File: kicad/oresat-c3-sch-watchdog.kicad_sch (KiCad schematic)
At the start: 20 parts

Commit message: Rough draft of watchdog and I2C system schematics.
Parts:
- added C112, C113: 10u, symbol Device:C_Small
- added R59: 1k, symbol Device:R_Small_US
- added R60, R61, R64: 100k, symbol Device:R_Small_US
- added R62: 47k, symbol Device:R_Small_US
- added R63: 470k, symbol Device:R_Small_US
- added R65: NP, symbol Device:R_Small_US
- added TP7, TP8, TP9: TestPoint-MinTH, oresat-misc:TestPoint-MinTH, symbol oresat-misc:TestPoint-MinTH
- added U28: TLV1704AIPWR, symbol oresat-ics:TLV1704AIPWR
- R31: value 10 -> 10 (1206)
- R41: value 10k -> 100k
- R58: value 10k -> 1k
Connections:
- net GND: now also C112.1, C113.1, U28.12 (V-)
- net VBUS: now also R65.2
- net at R34.2, R35.1: now also C113.2, U28.10 (-)
- net at R35.2, R36.1: now also U28.6 (-)
- net at R58.1: now also U28.2
- net at C111.2, R41.2, R58.2: now also TP7.1, U28.7 (+)
- net VP: now reaches R36.2, R37.1
- net VP: now also U28.5 (+)
- net VIN: now reaches C107.1, C108.1, C109.1, R31.2, R32.1, R41.1
- net VIN: now also R62.2, U28.3 (V+)
- net at R39.2: now also U28.4 (-)
- net at D3. (2): now also R60.2, R62.1, R63.1, TP9.1, U28.11 (+), U28.14
- net at R32.2, R34.1: now also R61.2
- net WDT renamed PET-WDT
- new net: D3. (2), R64.1
- new net: C112.2, R59.2, R63.2, R64.2, TP8.1, U28.8 (-)
- new net: R60.1, R61.1, U28.9 (+)
- new net: R59.1, U28.1
- new net ~{ORESAT-SD}: R65.1, U28.13
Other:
- note added: "CHANGE PERIOD TO 30 SEC"
- note added: "CHECK FOOTPRINT!!!"
- note added: "DC block and pulse detector"
- note added: "Keeps WDT circuit powered through ~{ORESAT-SD} asserted period (~ 2-3 seconds)"
- note added: "Oscillator"
- note added: "Output buffer"
- note added: "Pulse integrator"
- note removed: "1206"
- moved on the sheet: C107, C108, C109, C110, C111, D1, D3, D9, R31, R32, R34, R35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

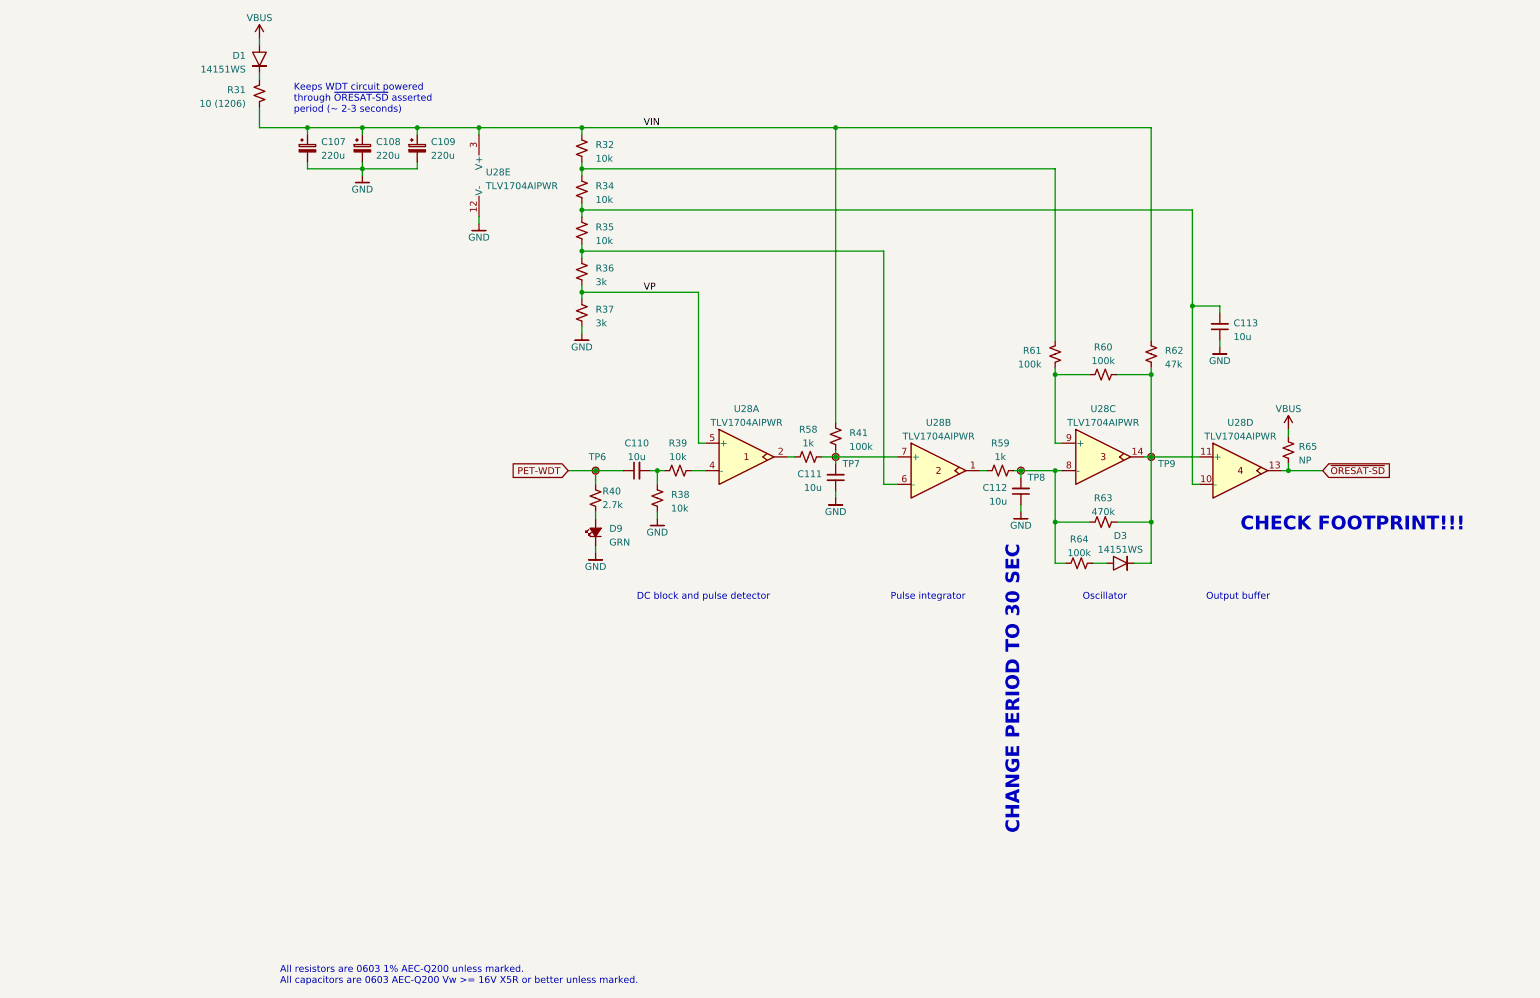
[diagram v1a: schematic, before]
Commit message: Simulated 30 second v6 watchdog circuit and fixed up watchdog in KiCAD.
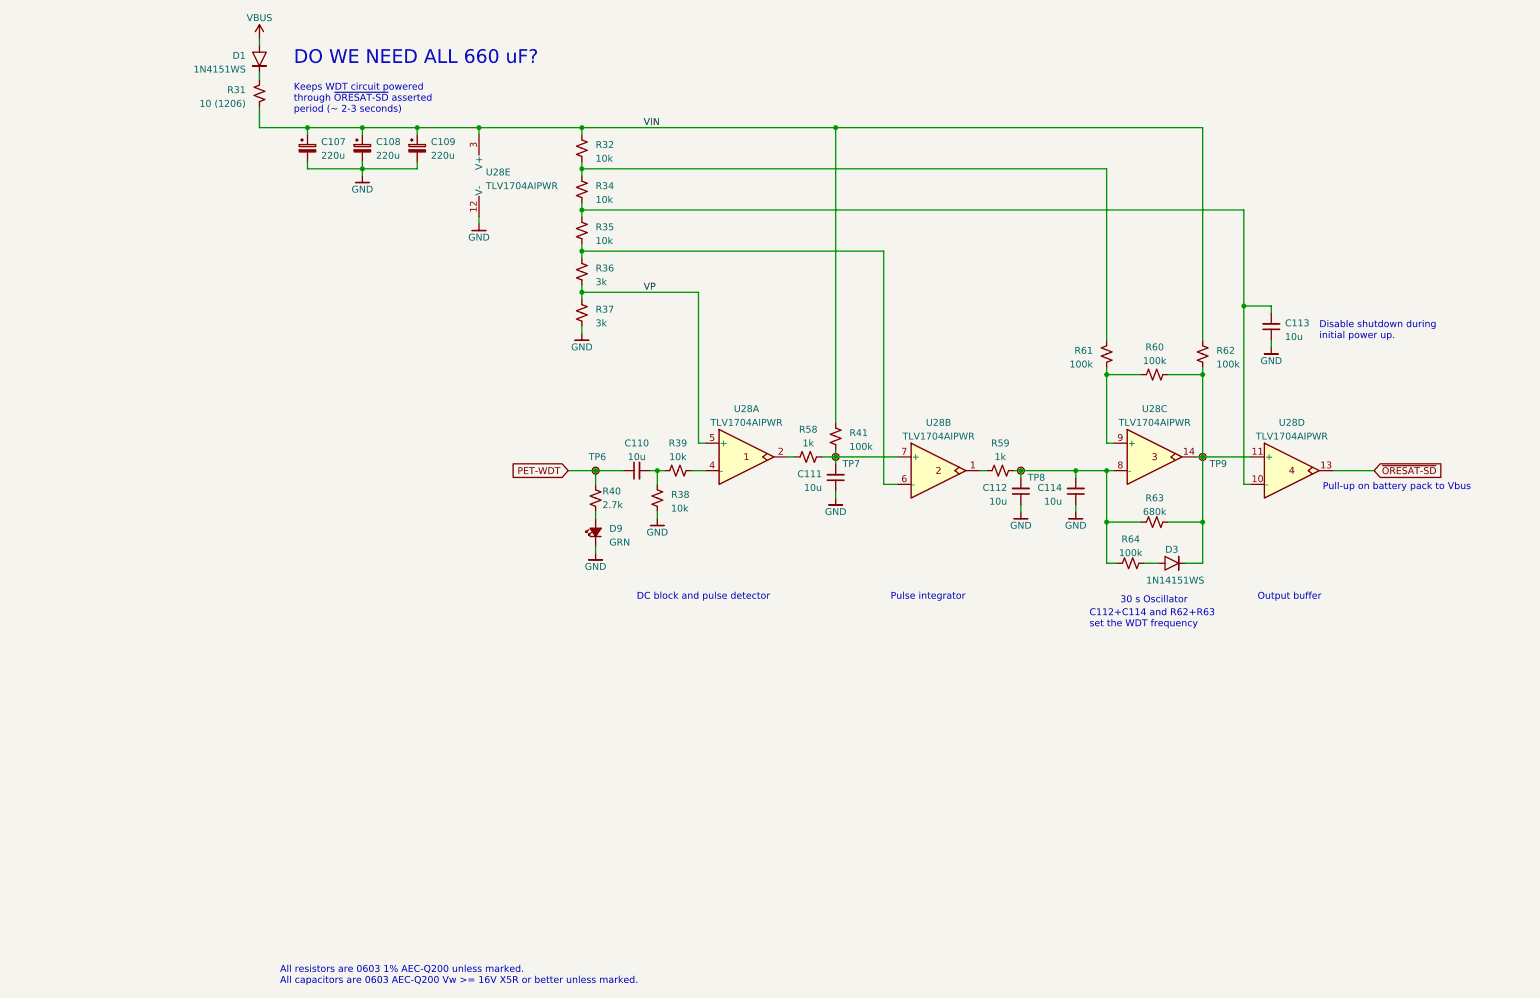
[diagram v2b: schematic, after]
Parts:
- removed R65: NP, symbol Device:R_Small_US
- added C114: 10u, symbol Device:C_Small
- D1: value 14151WS -> 1N4151WS
- D3: value 14151WS -> 1N14151WS
- R62: value 47k -> 100k
- R63: value 470k -> 680k
- U28: footprint (none) -> Package_SO:TSSOP-14_4.4x5mm_P0.65mm
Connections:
- net GND: now also C114.1
- net at C112.2, R59.2, R63.2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: now also C114.2
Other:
- note added: "30 s Oscillator"
- note added: "C112+C114 and R62+R63 set the WDT frequency"
- note added: "DO WE NEED ALL 660 uF?"
- note added: "Disable shutdown during initial power up."
- note added: "Pull-up on battery pack to Vbus"
- note removed: "CHANGE PERIOD TO 30 SEC"
- note removed: "CHECK FOOTPRINT!!!"
- note removed: "Oscillator"
- moved on the sheet: C113, D3, R60, R61, R62, R63, R64, TP9, U28C, U28D

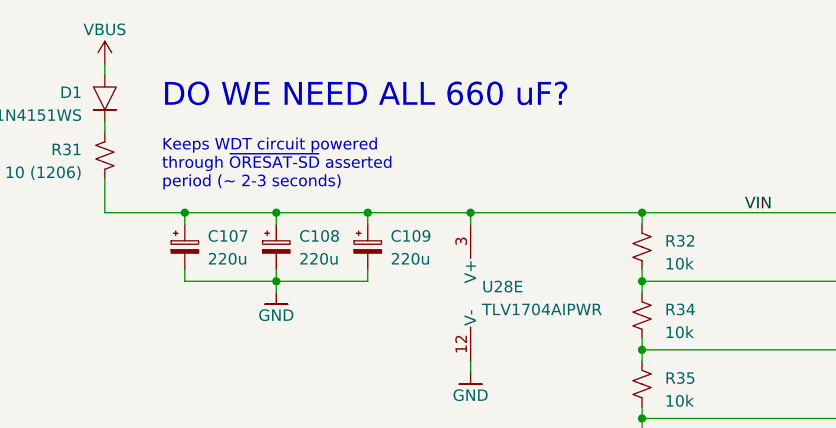
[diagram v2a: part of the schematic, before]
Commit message: C3 v6 schematic now 80% done. OSD2258 IC has been gone over with a fine tooth comb and simplified as much as possible. OSD3358 pinout compared to RED board and PocketBeagle. What's left: lots of little issues, footprints, and then L band and UHF radio schematics need to be fixed.
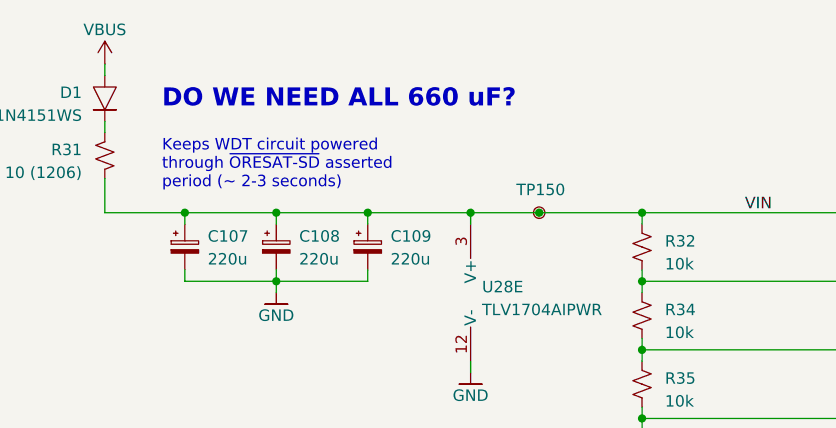
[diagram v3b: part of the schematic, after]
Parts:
- added TP150: TestPoint-MinTH, oresat-misc:TestPoint-MinTH, symbol oresat-misc:TestPoint-MinTH
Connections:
- net VIN: now also TP150.1
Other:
- title: Watchdog Circuit -> OreSat C3: Watchdog Circuit
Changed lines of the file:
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@@
   (paper "B")
   (title_block
-    (title "Watchdog Circuit")
-    (date "2023-05-02")
-    (rev "C3 v6.0")
+    (title "OreSat C3: Watchdog Circuit")
+    (date "2023-05-29")
+    (rev "6.0")
   )
   (junction (at 134.62 109.22) (diameter 0) (color 0 0 0 0)
@@
   (junction (at 272.415 174.625) (diameter 0) (color 0 0 0 0)
   )
+  (junction (at 163.83 101.6) (diameter 0) (color 0 0 0 0)
+  )
   (junction (at 297.815 134.62) (diameter 0) (color 0 0 0 0)
   )
@@
     (stroke (width 0) (type default))
   )
-  (wire (pts (xy 156.21 101.6) (xy 175.26 101.6))
+  (wire (pts (xy 156.21 101.6) (xy 163.83 101.6))
     (stroke (width 0) (type default))
   )
@@
   )
   (wire (pts (xy 175.26 124.46) (xy 231.14 124.46))
+    (stroke (width 0) (type default))
+  )
+  (wire (pts (xy 163.83 101.6) (xy 175.26 101.6))
     (stroke (width 0) (type default))
   )
@@
   )
   (text "DO WE NEED ALL 660 uF?" (at 121.92 90.17 0)
-    (effects (font (size 2.54 2.54) (color 255 0 0 1)) (justify left bottom))
+    (effects (font (size 2 2) (thickness 0.4) bold (color 255 0 0 1)) (justify left bottom))
   )
   (text "All resistors are 0603 1% AEC-Q200 unless marked.\nAll capacitors are 0603 AEC-Q200 Vw >= 16V X5R or better unless marked."
@@
     )
   )
+  (symbol (lib_id "oresat-misc:TestPoint-MinTH") (at 163.83 101.6 0) (unit 1)
+    (in_bom yes) (on_board yes) (dnp no)
+    (property "Reference" "TP150" (at 161.29 99.06 0)
+      (effects (font (size 1.27 1.27)) (justify left))
+    )
+    (property "Value" "TestPoint-MinTH" (at 163.83 94.615 0)
+      (effects (font (size 1.27 1.27)) hide)
+    )
+    (property "Footprint" "oresat-misc:TestPoint-MinTH" (at 163.83 96.52 0)
+      (effects (font (size 1.27 1.27)) hide)
+    )
+    (property "Datasheet" "" (at 163.83 101.6 0)
+      (effects (font (size 1.27 1.27)) hide)
+    )
+    (pin "1")
+    (instances
+      (project "oresat-c3"
+        (path "/65d12cdd-c326-4033-9053-c59fa4e0b25e/730a6f7e-0bbd-44c5-a45a-78e61e54b6d6"
+          (reference "TP150") (unit 1)
+        )
+      )
+    )
+  )
   (symbol (lib_id "Device:R_Small_US") (at 281.305 147.32 90) (unit 1)
     (in_bom yes) (on_board yes) (dnp no) (fields_autoplaced)
@@
     )
   )
-  (symbol (lib_id "oresat-ics:TLV1704AIPWR") (at 205.74 162.56 0) (unit 1)
+  (symbol (lib_name "TLV1704AIPWR_1") (lib_id "oresat-ics:TLV1704AIPWR") (at 205.74 162.56 0) (unit 1)
     (in_bom yes) (on_board yes) (dnp no) (fields_autoplaced)
     (property "Reference" "U28" (at 205.74 153.67 0)

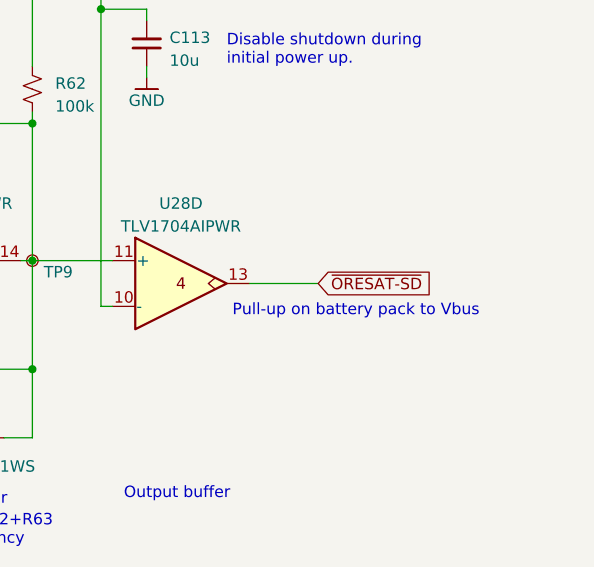
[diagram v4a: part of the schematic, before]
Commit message: Finished UHF radio schematic. Added sheet numbers to external labels. Still to do: L band radio, hooking up GPIO to the OSD3358, and test points.
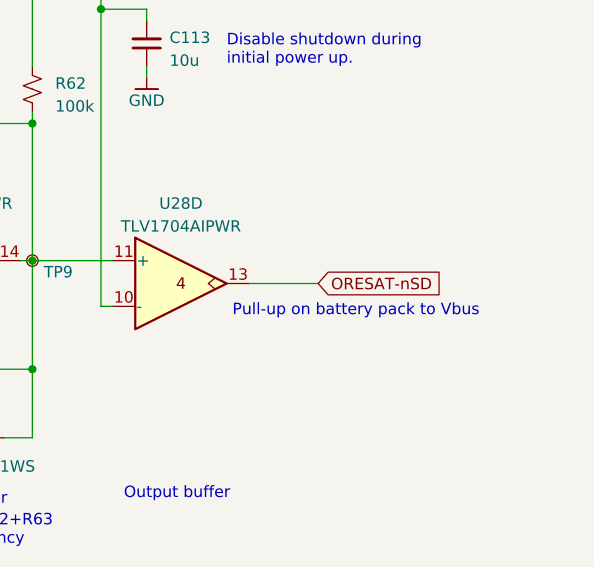
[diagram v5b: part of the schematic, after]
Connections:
- net ~{ORESAT-SD} renamed ORESAT-nSD
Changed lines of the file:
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@@
     (effects (font (size 1.27 1.27)) (justify right))
     (property "Intersheetrefs" "${INTERSHEET_REFS}" (at 161.1662 165.1 0)
-      (effects (font (size 1.27 1.27)) (justify right) hide)
+      (effects (font (size 1.27 1.27)) (justify right))
     )
   )
-  (global_label "~{ORESAT-SD}" (shape input) (at 321.945 165.1 0) (fields_autoplaced)
+  (global_label "ORESAT-nSD" (shape input) (at 321.945 165.1 0) (fields_autoplaced)
     (effects (font (size 1.27 1.27)) (justify left))
-    (property "Intersheetrefs" "${INTERSHEET_REFS}" (at 335.9179 165.1 0)
-      (effects (font (size 1.27 1.27)) (justify left) hide)
+    (property "Intersheetrefs" "${INTERSHEET_REFS}" (at 337.0669 165.1 0)
+      (effects (font (size 1.27 1.27)) (justify left))
     )
   )

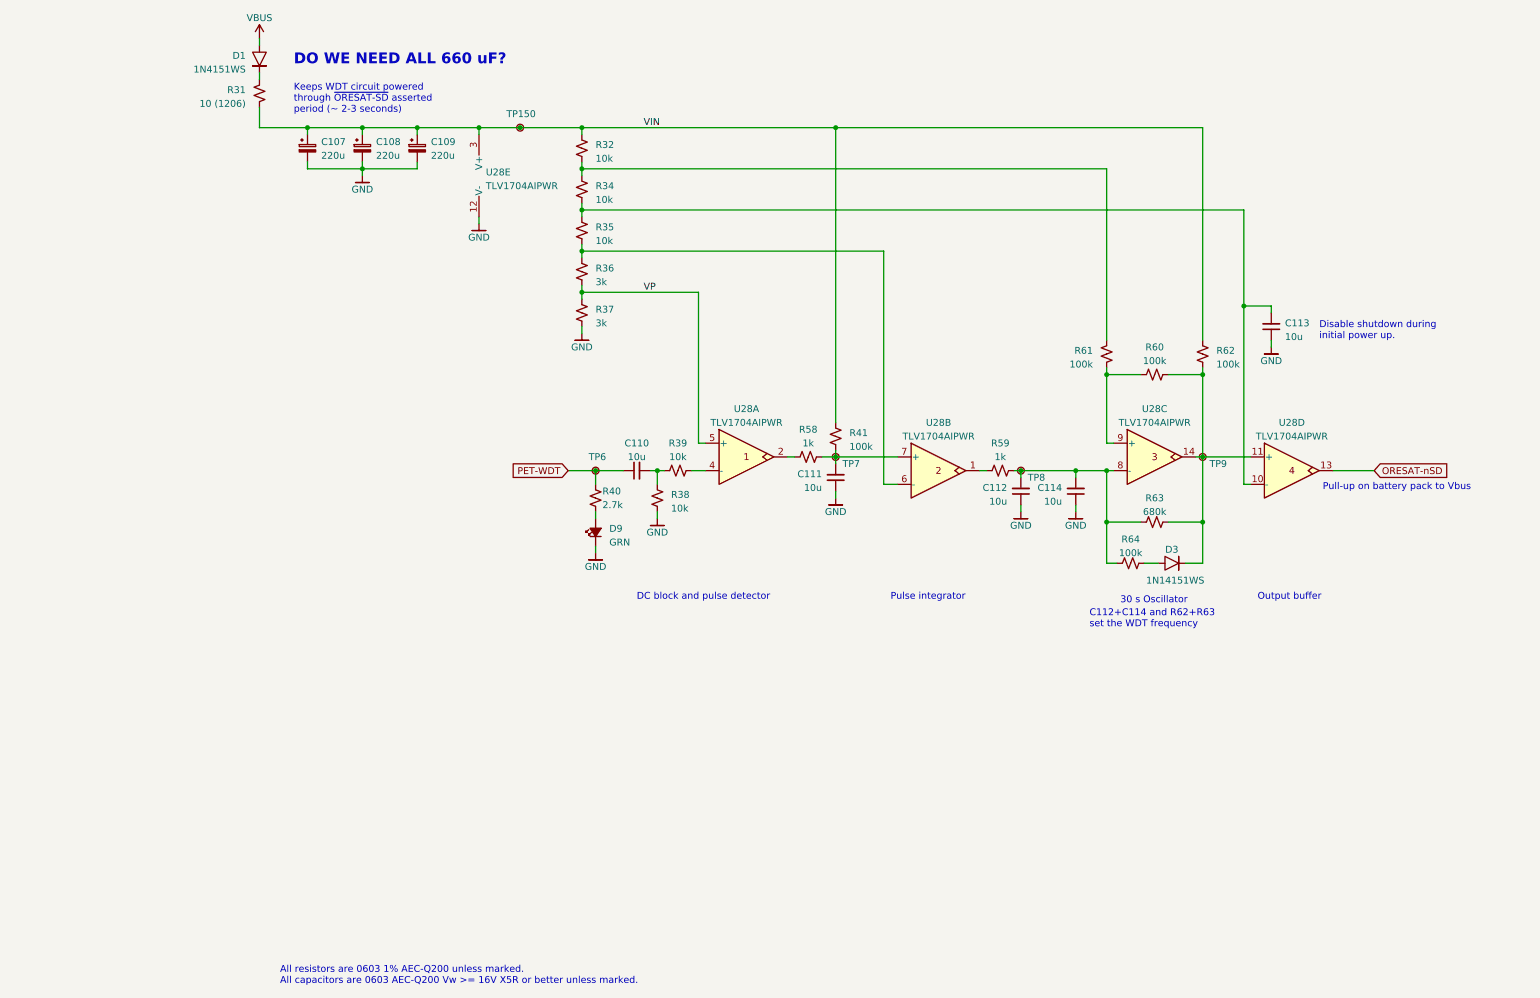
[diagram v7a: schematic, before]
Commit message: First round of ERC fixes.
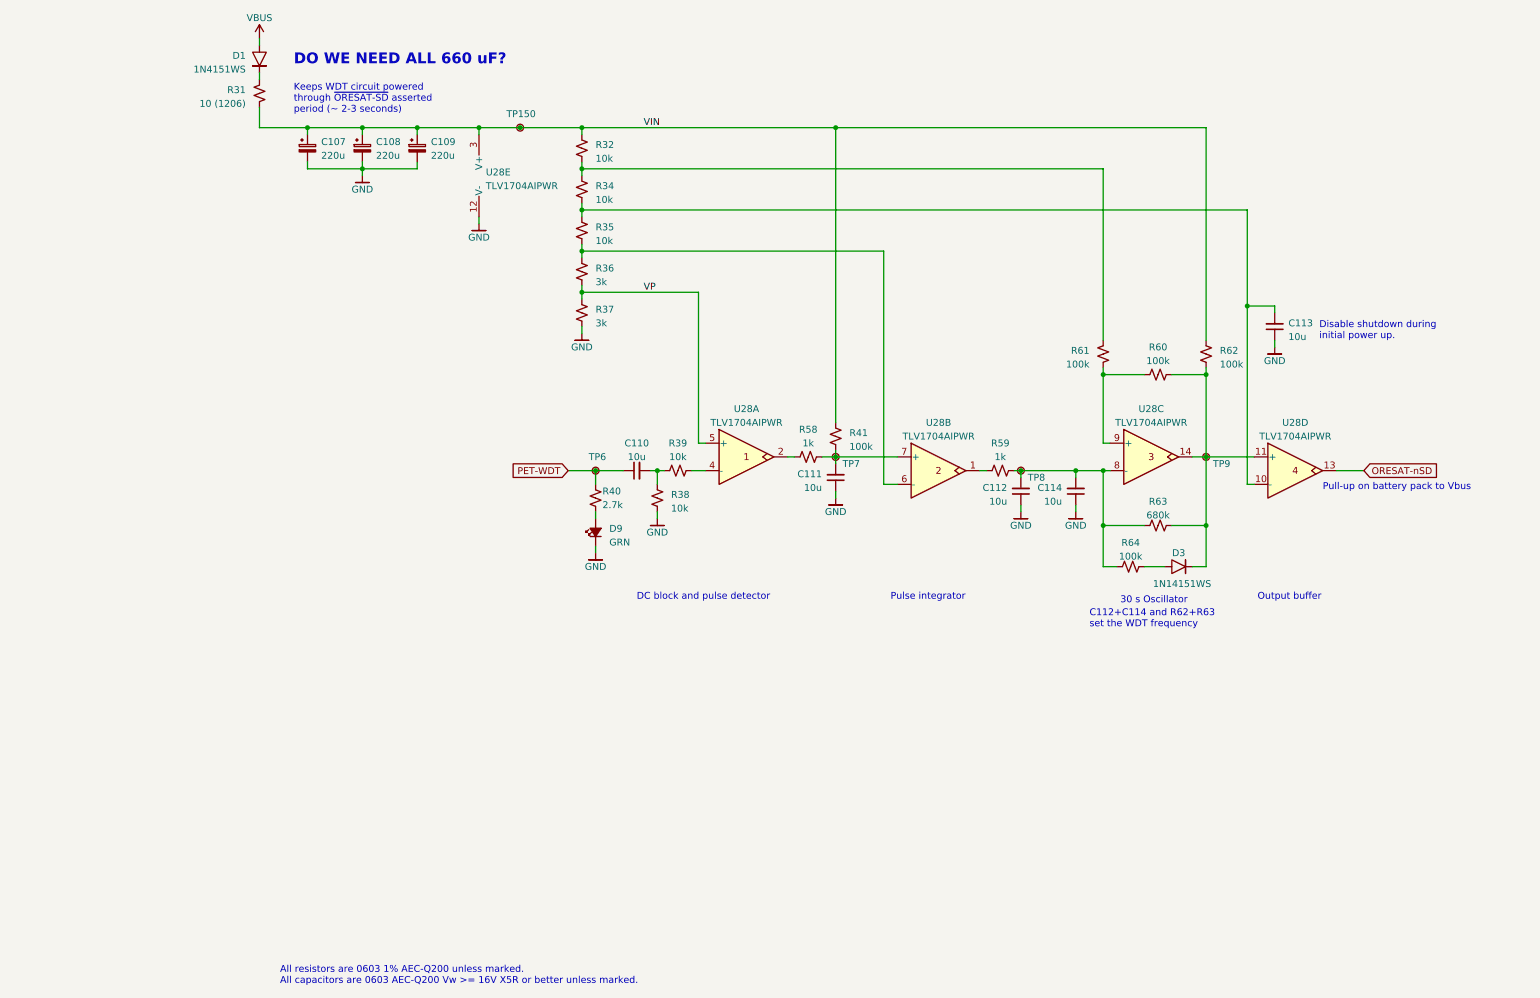
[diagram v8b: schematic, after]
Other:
- moved on the sheet: C113, D3, R60, R61, R62, R63, R64, TP9, U28C, U28D
